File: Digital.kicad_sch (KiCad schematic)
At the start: 9 parts, among them U5 NLSX4373DR2G, U6 CAT3200-5

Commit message: Basically done with schematic, will split to different PCBs now
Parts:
- C23, C24, C25, C26, C31, JP1: footprint (none) -> Capacitor_SMD:C_0805_2012Metric
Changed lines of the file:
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@@
       (effects (font (size 1.27 1.27)) (justify left))
     )
-    (property "Footprint" "" (at 160.02 57.15 0)
+    (property "Footprint" "Capacitor_SMD:C_0805_2012Metric" (at 160.02 57.15 0)
       (effects (font (size 1.27 1.27)) hide)
     )
@@
       (effects (font (size 1.27 1.27)) (justify left))
     )
-    (property "Footprint" "" (at 123.19 57.15 0)
+    (property "Footprint" "Capacitor_SMD:C_0805_2012Metric" (at 123.19 57.15 0)
       (effects (font (size 1.27 1.27)) hide)
     )
@@
       (effects (font (size 1.27 1.27)) (justify left))
     )
-    (property "Footprint" "" (at 198.12 81.915 0)
+    (property "Footprint" "Capacitor_SMD:C_0805_2012Metric" (at 198.12 81.915 0)
       (effects (font (size 1.27 1.27)) hide)
     )
@@
       (effects (font (size 1.27 1.27)))
     )
-    (property "Footprint" "" (at 123.19 46.99 0)
+    (property "Footprint" "Capacitor_SMD:C_0805_2012Metric" (at 123.19 46.99 0)
       (effects (font (size 1.27 1.27)) hide)
     )
@@
       (effects (font (size 1.27 1.27)) (justify left))
     )
-    (property "Footprint" "" (at 163.195 88.265 0)
+    (property "Footprint" "Capacitor_SMD:C_0805_2012Metric" (at 163.195 88.265 0)
       (effects (font (size 1.27 1.27)) hide)
     )
@@
       (effects (font (size 1.27 1.27)) (justify left))
     )
-    (property "Footprint" "" (at 131.445 64.77 0)
-      (effects (font (size 1.27 1.27)) hide)
-    )
+    (property "Footprint" "Capacitor_SMD:C_0805_2012Metric" (at 131.445 64.77 0)
+      (effects (font (size 1.27 1.27)) hide)
+    )

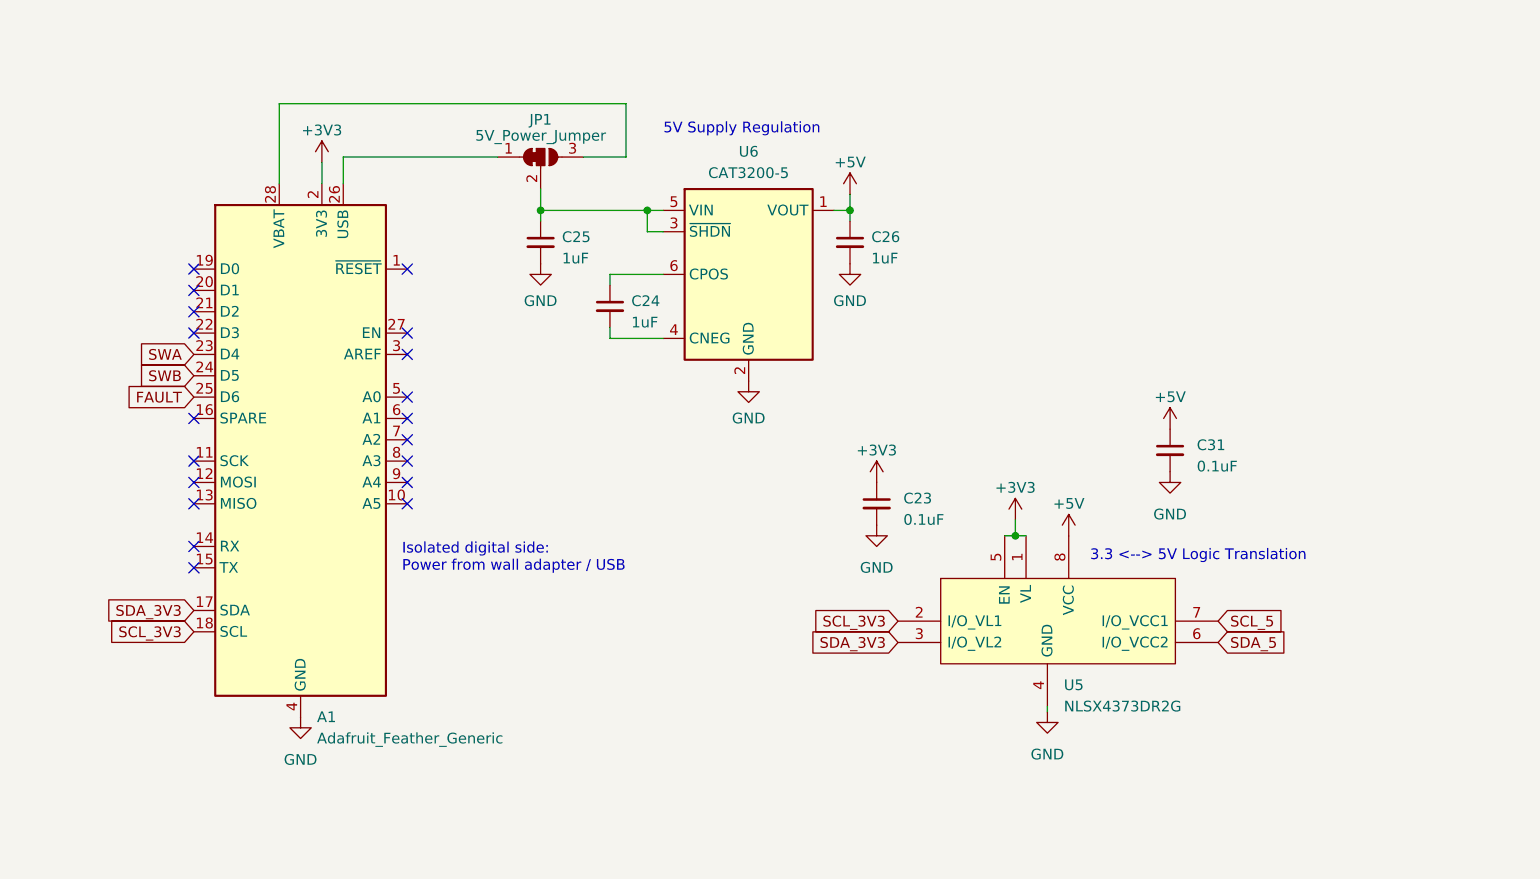
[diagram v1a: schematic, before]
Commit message: Finished footprint assignment
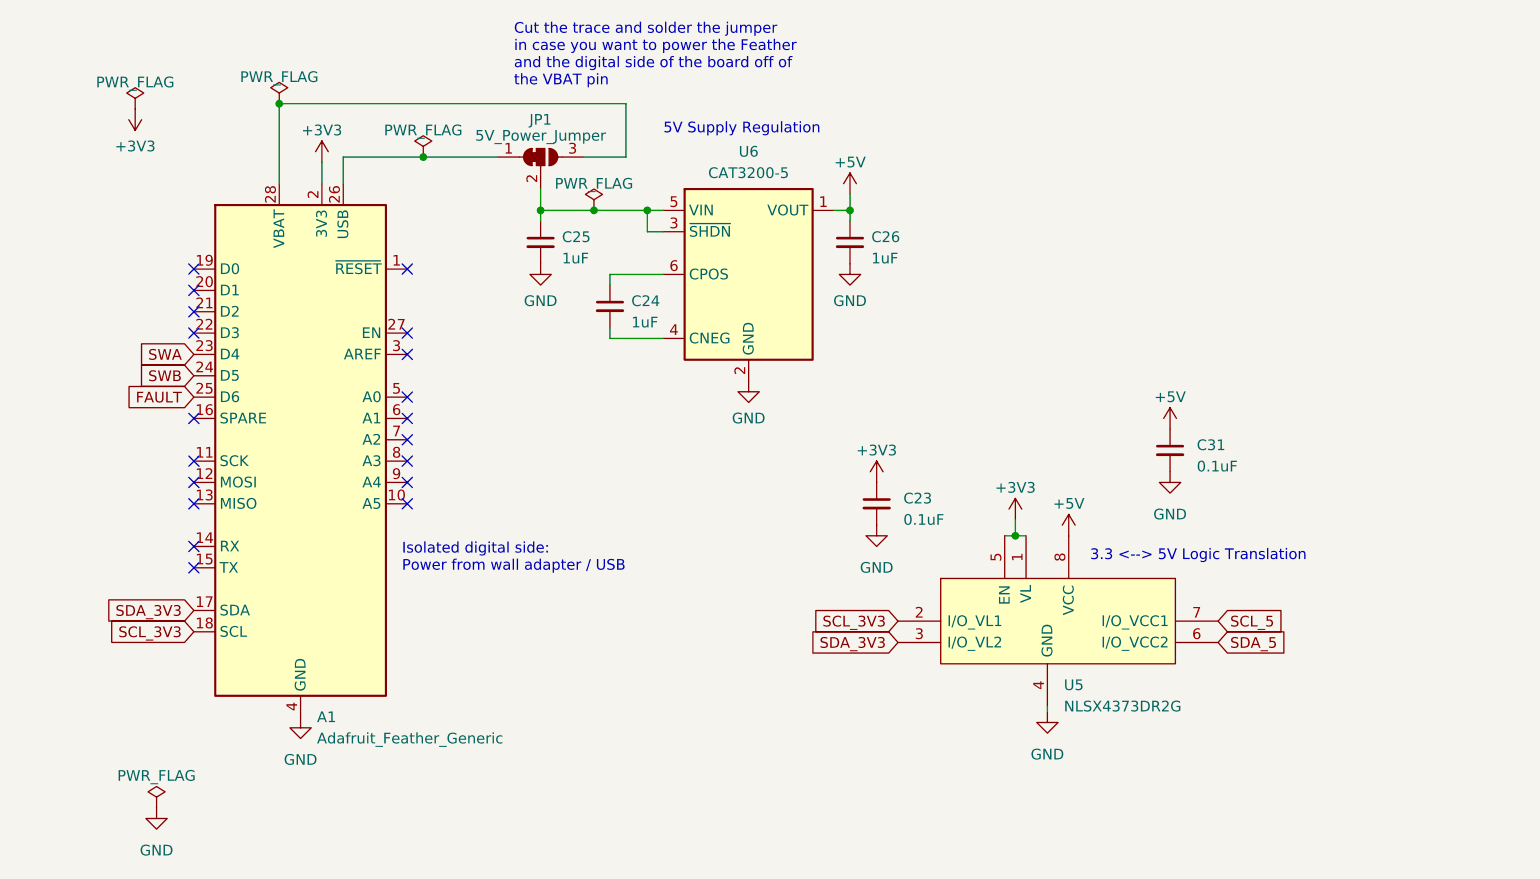
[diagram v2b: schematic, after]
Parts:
- JP1: footprint Capacitor_SMD:C_0805_2012Metric -> Jumper:SolderJumper-3_P1.3mm_Bridged2Bar12_RoundedPad1.0x1.5mm
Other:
- note added: "Cut the trace and solder the jumper in case you want to power the Feather and the digital side of the board off of the VBAT pin"
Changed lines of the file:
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@@
   (junction (at 123.19 53.34) (diameter 0) (color 0 0 0 0)
   )
+  (junction (at 129.54 53.34) (diameter 0) (color 0 0 0 0)
+  )
+  (junction (at 109.22 46.99) (diameter 0) (color 0 0 0 0)
+  )
   (junction (at 160.02 53.34) (diameter 0) (color 0 0 0 0)
   )
   (junction (at 179.705 92.075) (diameter 0) (color 0 0 0 0)
+  )
+  (junction (at 92.075 40.64) (diameter 0) (color 0 0 0 0)
   )
   (no_connect (at 107.315 60.325))
@@
   (no_connect (at 81.915 85.725))
   (no_connect (at 81.915 62.865))
-  (wire (pts (xy 99.695 46.99) (xy 118.11 46.99))
+  (wire (pts (xy 99.695 46.99) (xy 109.22 46.99))
     (stroke (width 0) (type default))
   )
@@
     (stroke (width 0) (type default))
   )
+  (wire (pts (xy 129.54 53.34) (xy 135.89 53.34))
+    (stroke (width 0) (type default))
+  )
   (wire (pts (xy 123.19 50.8) (xy 123.19 53.34))
     (stroke (width 0) (type default))
   )
-  (wire (pts (xy 123.19 53.34) (xy 135.89 53.34))
+  (wire (pts (xy 123.19 53.34) (xy 129.54 53.34))
     (stroke (width 0) (type default))
   )
@@
   )
   (wire (pts (xy 92.075 40.64) (xy 92.075 50.165))
+    (stroke (width 0) (type default))
+  )
+  (wire (pts (xy 109.22 46.99) (xy 118.11 46.99))
     (stroke (width 0) (type default))
   )
@@
   )
   (text "5V Supply Regulation" (at 137.795 44.45 0)
+    (effects (font (size 1.27 1.27)) (justify left bottom))
+  )
+  (text "Cut the trace and solder the jumper\nin case you want to power the Feather\nand the digital side of the board off of\nthe VBAT pin"
+    (at 120.015 38.735 0)
     (effects (font (size 1.27 1.27)) (justify left bottom))
   )
@@
     (property "Intersheetrefs" "${INTERSHEET_REFS}" (at 71.0264 103.505 0)
       (effects (font (size 1.27 1.27)) (justify right) hide)
+    )
+  )
+  (symbol (lib_id "power:PWR_FLAG") (at 77.47 124.46 0) (unit 1)
+    (in_bom yes) (on_board yes) (dnp no) (fields_autoplaced)
+    (property "Reference" "#FLG06" (at 77.47 122.555 0)
+      (effects (font (size 1.27 1.27)) hide)
+    )
+    (property "Value" "PWR_FLAG" (at 77.47 120.65 0)
+      (effects (font (size 1.27 1.27)))
+    )
+    (property "Footprint" "" (at 77.47 124.46 0)
+      (effects (font (size 1.27 1.27)) hide)
+    )
+    (property "Datasheet" "~" (at 77.47 124.46 0)
+      (effects (font (size 1.27 1.27)) hide)
+    )
+    (pin "1")
+    (instances
+      (project "AMF-Generator"
+        (path "/c3df021c-646c-4a68-ac14-a081c2121d02/deb1fbb3-49ca-4dbd-9206-e1712cc02a38"
+          (reference "#FLG06") (unit 1)
+        )
+      )
     )
   )
@@
     )
   )
+  (symbol (lib_id "power:PWR_FLAG") (at 74.93 41.275 0) (unit 1)
+    (in_bom yes) (on_board yes) (dnp no) (fields_autoplaced)
+    (property "Reference" "#FLG07" (at 74.93 39.37 0)
+      (effects (font (size 1.27 1.27)) hide)
+    )
+    (property "Value" "PWR_FLAG" (at 74.93 38.1 0)
+      (effects (font (size 1.27 1.27)))
+    )
+    (property "Footprint" "" (at 74.93 41.275 0)
+      (effects (font (size 1.27 1.27)) hide)
+    )
+    (property "Datasheet" "~" (at 74.93 41.275 0)
+      (effects (font (size 1.27 1.27)) hide)
+    )
+    (pin "1")
+    (instances
+      (project "AMF-Generator"
+        (path "/c3df021c-646c-4a68-ac14-a081c2121d02/deb1fbb3-49ca-4dbd-9206-e1712cc02a38"
+          (reference "#FLG07") (unit 1)
+        )
+      )
+    )
+  )
   (symbol (lib_id "Device:C_Small") (at 160.02 57.15 0) (unit 1)
     (in_bom yes) (on_board yes) (dnp no) (fields_autoplaced)
@@
         (path "/c3df021c-646c-4a68-ac14-a081c2121d02/deb1fbb3-49ca-4dbd-9206-e1712cc02a38"
           (reference "#PWR046") (unit 1)
+        )
+      )
+    )
+  )
+  (symbol (lib_id "power:PWR_FLAG") (at 129.54 53.34 0) (unit 1)
+    (in_bom yes) (on_board yes) (dnp no) (fields_autoplaced)
+    (property "Reference" "#FLG05" (at 129.54 51.435 0)
+      (effects (font (size 1.27 1.27)) hide)
+    )
+    (property "Value" "PWR_FLAG" (at 129.54 50.165 0)
+      (effects (font (size 1.27 1.27)))
+    )
+    (property "Footprint" "" (at 129.54 53.34 0)
+      (effects (font (size 1.27 1.27)) hide)
+    )
+    (property "Datasheet" "~" (at 129.54 53.34 0)
+      (effects (font (size 1.27 1.27)) hide)
+    )
+    (pin "1")
+    (instances
+      (project "AMF-Generator"
+        (path "/c3df021c-646c-4a68-ac14-a081c2121d02/deb1fbb3-49ca-4dbd-9206-e1712cc02a38"
+          (reference "#FLG05") (unit 1)
         )
       )
@@
       (effects (font (size 1.27 1.27)))
     )
-    (property "Footprint" "Capacitor_SMD:C_0805_2012Metric" (at 123.19 46.99 0)
+    (property "Footprint" "Jumper:SolderJumper-3_P1.3mm_Bridged2Bar12_RoundedPad1.0x1.5mm" (at 123.19 46.99 0)
       (effects (font (size 1.27 1.27)) hide)
     )
@@
     )
   )
+  (symbol (lib_id "power:GND") (at 77.47 124.46 0) (unit 1)
+    (in_bom yes) (on_board yes) (dnp no) (fields_autoplaced)
+    (property "Reference" "#PWR04" (at 77.47 130.81 0)
+      (effects (font (size 1.27 1.27)) hide)
+    )
+    (property "Value" "GND" (at 77.47 129.54 0)
+      (effects (font (size 1.27 1.27)))
+    )
+    (property "Footprint" "" (at 77.47 124.46 0)
+      (effects (font (size 1.27 1.27)) hide)
+    )
+    (property "Datasheet" "" (at 77.47 124.46 0)
+      (effects (font (size 1.27 1.27)) hide)
+    )
+    (pin "1")
+    (instances
+      (project "AMF-Generator"
+        (path "/c3df021c-646c-4a68-ac14-a081c2121d02"
+          (reference "#PWR04") (unit 1)
+        )
+        (path "/c3df021c-646c-4a68-ac14-a081c2121d02/deb1fbb3-49ca-4dbd-9206-e1712cc02a38"
+          (reference "#PWR064") (unit 1)
+        )
+      )
+    )
+  )
   (symbol (lib_id "power:GND") (at 94.615 113.665 0) (unit 1)
     (in_bom yes) (on_board yes) (dnp no) (fields_autoplaced)
@@
     )
   )
+  (symbol (lib_id "power:+3V3") (at 74.93 41.275 180) (unit 1)
+    (in_bom yes) (on_board yes) (dnp no) (fields_autoplaced)
+    (property "Reference" "#PWR018" (at 74.93 37.465 0)
+      (effects (font (size 1.27 1.27)) hide)
+    )
+    (property "Value" "+3V3" (at 74.93 45.72 0)
+      (effects (font (size 1.27 1.27)))
+    )
+    (property "Footprint" "" (at 74.93 41.275 0)
+      (effects (font (size 1.27 1.27)) hide)
+    )
+    (property "Datasheet" "" (at 74.93 41.275 0)
+      (effects (font (size 1.27 1.27)) hide)
+    )
+    (pin "1")
+    (instances
+      (project "AMF-Generator"
+        (path "/c3df021c-646c-4a68-ac14-a081c2121d02"
+          (reference "#PWR018") (unit 1)
+        )
+        (path "/c3df021c-646c-4a68-ac14-a081c2121d02/deb1fbb3-49ca-4dbd-9206-e1712cc02a38"
+          (reference "#PWR065") (unit 1)
+        )
+      )
+    )
+  )
   (symbol (lib_id "Device:C_Small") (at 163.195 88.265 0) (unit 1)
     (in_bom yes) (on_board yes) (dnp no) (fields_autoplaced)
@@
         (path "/c3df021c-646c-4a68-ac14-a081c2121d02/deb1fbb3-49ca-4dbd-9206-e1712cc02a38"
           (reference "#PWR018") (unit 1)
+        )
+      )
+    )
+  )
+  (symbol (lib_id "power:PWR_FLAG") (at 92.075 40.64 0) (unit 1)
+    (in_bom yes) (on_board yes) (dnp no) (fields_autoplaced)
+    (property "Reference" "#FLG03" (at 92.075 38.735 0)
+      (effects (font (size 1.27 1.27)) hide)
+    )
+    (property "Value" "PWR_FLAG" (at 92.075 37.465 0)
+      (effects (font (size 1.27 1.27)))
+    )
+    (property "Footprint" "" (at 92.075 40.64 0)
+      (effects (font (size 1.27 1.27)) hide)
+    )
+    (property "Datasheet" "~" (at 92.075 40.64 0)
+      (effects (font (size 1.27 1.27)) hide)
+    )
+    (pin "1")
+    (instances
+      (project "AMF-Generator"
+        (path "/c3df021c-646c-4a68-ac14-a081c2121d02/deb1fbb3-49ca-4dbd-9206-e1712cc02a38"
+          (reference "#FLG03") (unit 1)
         )
       )
@@
         )
       )
+    )
+  )
+  (symbol (lib_id "power:PWR_FLAG") (at 109.22 46.99 0) (unit 1)
+    (in_bom yes) (on_board yes) (dnp no) (fields_autoplaced)
+    (property "Reference" "#FLG04" (at 109.22 45.085 0)
+      (effects (font (size 1.27 1.27)) hide)
+    )
+    (property "Value" "PWR_FLAG" (at 109.22 43.815 0)
+      (effects (font (size 1.27 1.27)))
+    )
+    (property "Footprint" "" (at 109.22 46.99 0)
+      (effects (font (size 1.27 1.27)) hide)
+    )
+    (property "Datasheet" "~" (at 109.22 46.99 0)
+      (effects (font (size 1.27 1.27)) hide)
+    )
+    (pin "1")
+    (instances
+      (project "AMF-Generator"
+        (path "/c3df021c-646c-4a68-ac14-a081c2121d02/deb1fbb3-49ca-4dbd-9206-e1712cc02a38"
+          (reference "#FLG04") (unit 1)
+        )
+      )

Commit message: Initial pass of component placement complete. Added test points and i2c headers, also changed 12V input to terminal block
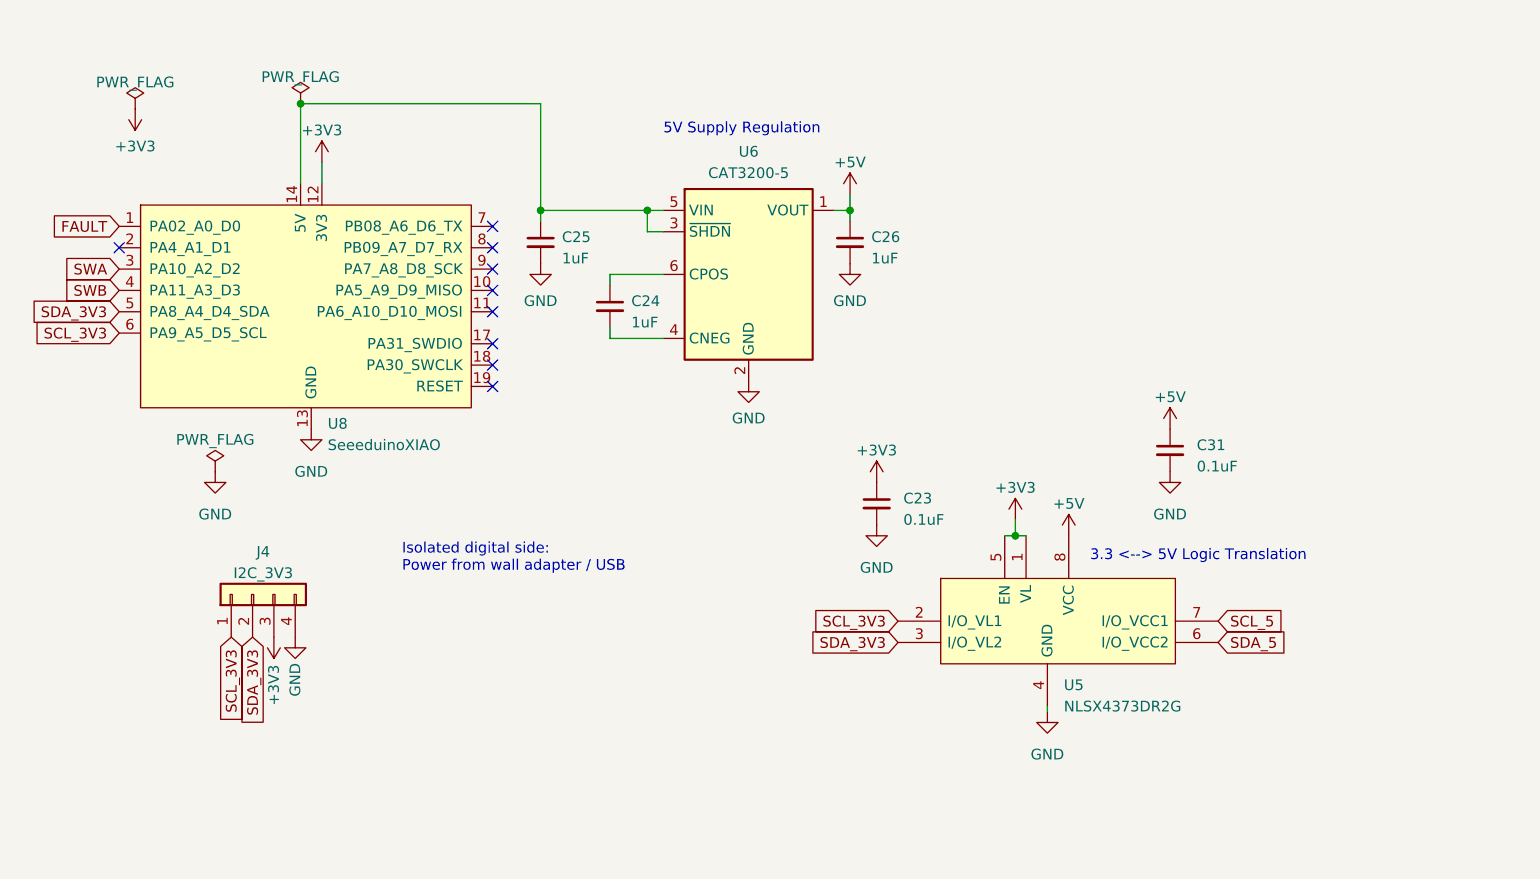
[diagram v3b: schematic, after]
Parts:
- removed A1: Adafruit_Feather_Generic, Module:Adafruit_Feather, symbol MCU_Module:Adafruit_Feather_Generic
- removed JP1: 5V_Power_Jumper, Jumper:SolderJumper-3_P1.3mm_Bridged2Bar12_RoundedPad1.0x1.5mm, symbol Jumper:SolderJumper_3_Bridged12
- added J4: I2C_3V3, Connector_PinHeader_2.54mm:PinHeader_1x04_P2.54mm_Vertical, symbol Connector_Generic:Conn_01x04
- added U8: SeeeduinoXIAO, Seeeduino XIAO KICAD:Seeeduino XIAO-MOUDLE14P-2.54-21X17.8MM, symbol Seeeduino XIAO:SeeeduinoXIAO
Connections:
- net +3V3: now also J4.3 (Pin_3), U8.12 (3V3)
- net FAULT: now also U8.1 (PA02_A0_D0)
- net GND: now also J4.4 (Pin_4), U8.13 (GND), U8.20 (GND)
- net SCL_3V3: now also J4.1 (Pin_1), U8.6 (PA9_A5_D5_SCL)
- net SDA_3V3: now also J4.2 (Pin_2), U8.5 (PA8_A4_D4_SDA)
- net SWA: now also U8.3 (PA10_A2_D2)
- net SWB: now also U8.4 (PA11_A3_D3)
- net at C25.1, U6.3 (~{SHDN}), U6.5 (VIN): now also U8.14 (5V)
- no-connect marks 19 -> 9
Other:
- note removed: "Cut the trace and solder the jumper in case you want to power the Feather and the digital side of the board off of the VBAT pin"

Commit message: initial pass of layout complete
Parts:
- removed U8: SeeeduinoXIAO, Seeeduino XIAO KICAD:Seeeduino XIAO-MOUDLE14P-2.54-21X17.8MM, symbol Seeeduino XIAO:SeeeduinoXIAO
- added D3 (x2): LED, LED_SMD:LED_0805_2012Metric, symbol Device:LED
- added R9: 600, Resistor_SMD:R_0805_2012Metric, symbol Device:R
- added R9: 260, Resistor_SMD:R_0805_2012Metric, symbol Device:R
- added U9: QTPY, QTPY:QTPY-RP2040, symbol QTPY:QTPY
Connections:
- net +3V3: now also R9.1, U9.10 (3.3V)
- net +5V: now also R9.1
- net FAULT: now also U9.1 (A0)
- net GND: now also D3.1 (K), D3.1 (K), U9.9 (GND)
- net SCL_3V3: now also U9.6 (SCL)
- net SDA_3V3: now also U9.5 (SDA)
- net at C25.1, U6.3 (~{SHDN}), U6.5 (VIN): now also U9.8 (5V)
- new net: D3.2 (A), R9.2 (x2)
- new net PWM_A: U9.3 (A2)
- new net PWM_B: U9.4 (A3)
- no-connect marks 9 -> 6
